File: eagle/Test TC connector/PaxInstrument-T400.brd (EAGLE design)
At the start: 99.1 x 50.8 mm, 134 parts, among them IC1 MCP3424, IC3 SN74LVC1G74DCT, J1 MICRO-SDCARD-CONNECTOR-330006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, Q1 DMP2035U-7, Q2 DMP2035U-7, Q3 DMN2075U-7, Q4 DMN2075U-7, Q5 DMP2035U-7, U1 MCP9800, U2 APX809, U3 MCP73831, U4 MIC5219-3.3V, X1 FH12-12S-1S, Y1 RESONATORSMD

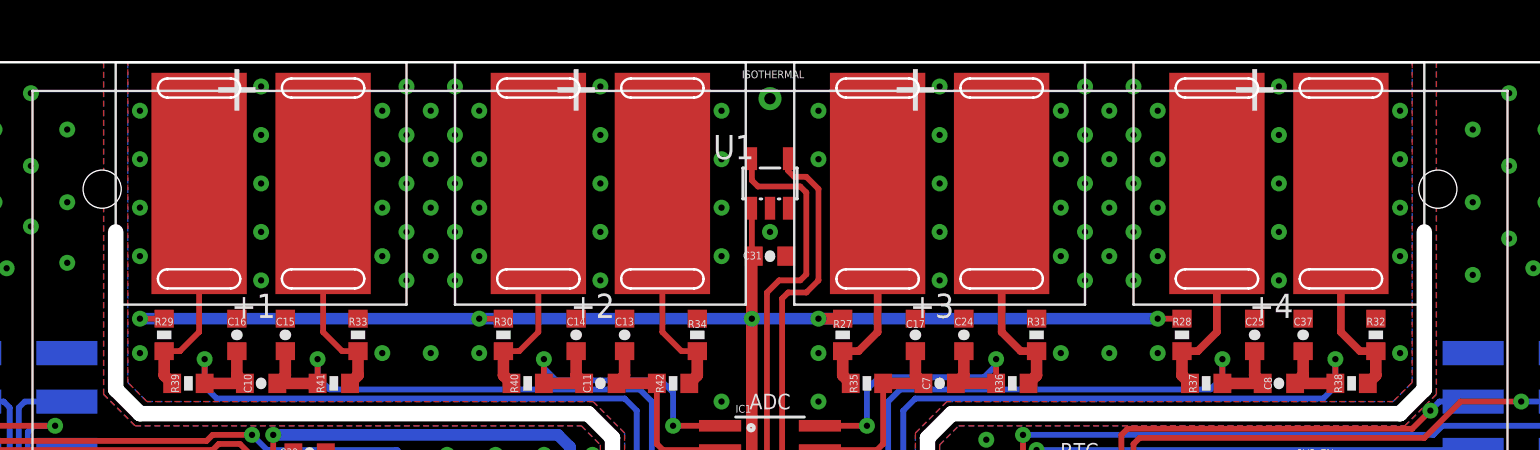
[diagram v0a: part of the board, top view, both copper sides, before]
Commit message: Added new TC connector
Thermocouple connector footprint #170
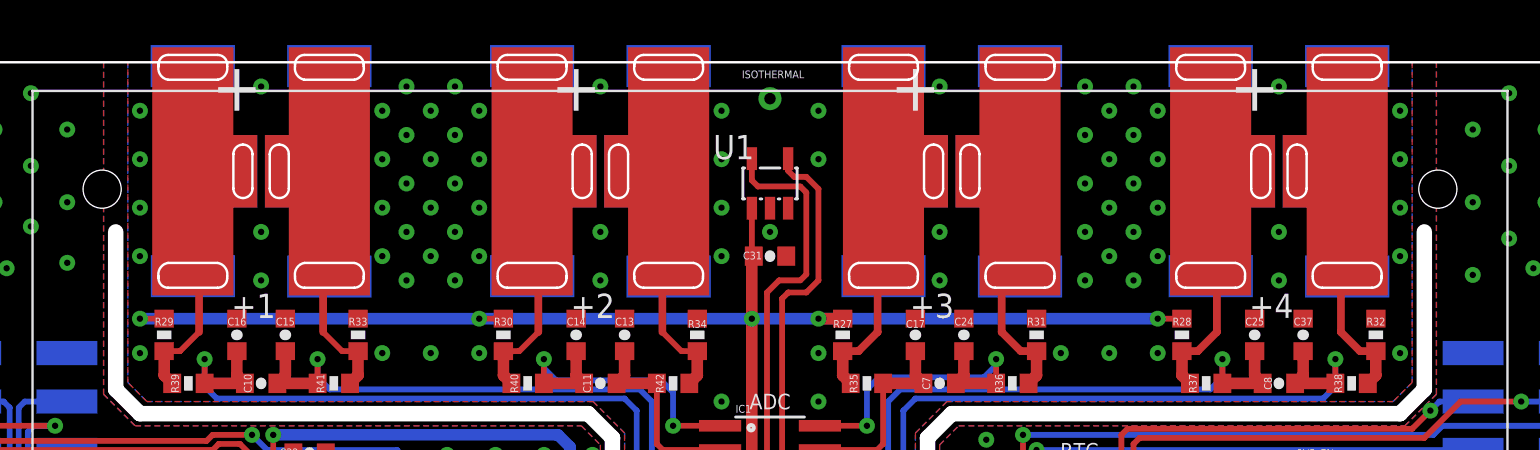
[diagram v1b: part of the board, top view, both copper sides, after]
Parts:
- U$10, U$11, U$12, U$13: value CHARLESPAX_TC-MINI-CONNECTOR -> TC-MINI-CONNECTOR1024; device PaxInstrument-T400:CHARLESPAX_TC-MINI-CONNECTOR -> PaxInstruments-Connectors:1024-TC-CONNECTOR
- moved U$10 0.90 mm to (57.8, 45.1), turned to 0 degrees
- moved U$11 0.63 mm to (74.9, 45.1), turned to 0 degrees
- moved U$12 0.63 mm to (21.6, 45.1), turned to 0 degrees
- moved U$13 0.63 mm to (39.4, 45.1), turned to 0 degrees
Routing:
- net N$5: track 11.9 -> 13.5 mm
- net N$40: track 11.9 -> 12.9 mm
- net N$35: track 11.9 -> 12.9 mm
- net N$16: track 11.9 -> 12.9 mm
- net N$14: track 11.9 -> 12.9 mm
- net N$13: track 11.9 -> 12.9 mm
- net N$34: track 11.9 -> 12.9 mm
- net N$11: track 11.9 -> 12.8 mm
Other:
- board text added: "Test TC connector 1024"
